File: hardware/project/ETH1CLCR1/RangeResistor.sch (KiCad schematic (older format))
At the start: 107 parts, among them K801 TQ2SA-5V, Q801 BC847W, Q802 2N2218A, Q803 2N2904A, Q804 BC847W, Q805 BC847W, Q806 BC847W, Q807 BC847W, Q808 BC847W, U801 TL072, U802 AD5293BRUZ-20, U803 AQY212GS, U804 HA3-2525-5Z, U805 AQY212GS, U806 AQY212GS, U807 AQY212GS, U808 AQY212GS, U809 AQY212GS, U810 AQY212GS, U811 AQY212GS, U812 AQY212GS, U813 AQY212GS, U814 AQY212GS, U815 AQY212GS

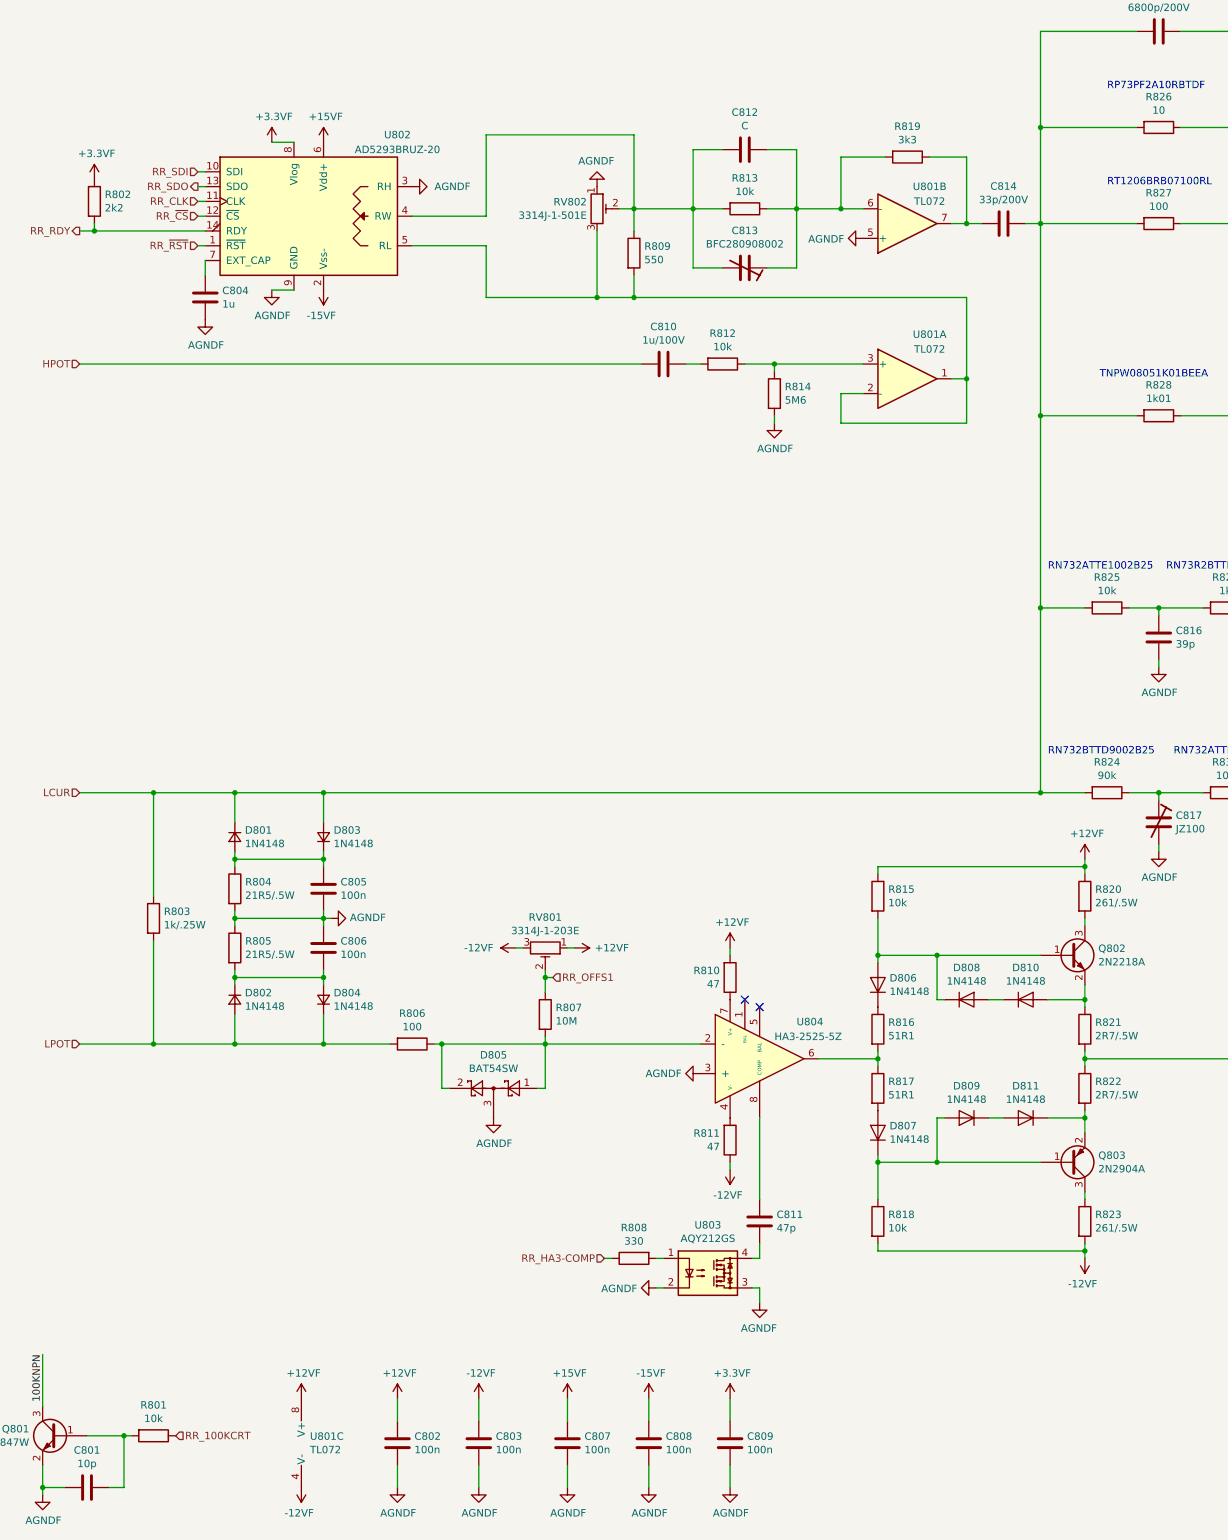
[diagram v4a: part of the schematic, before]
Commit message: Fixed some mistakes in the foorpeints. BOM list ready.
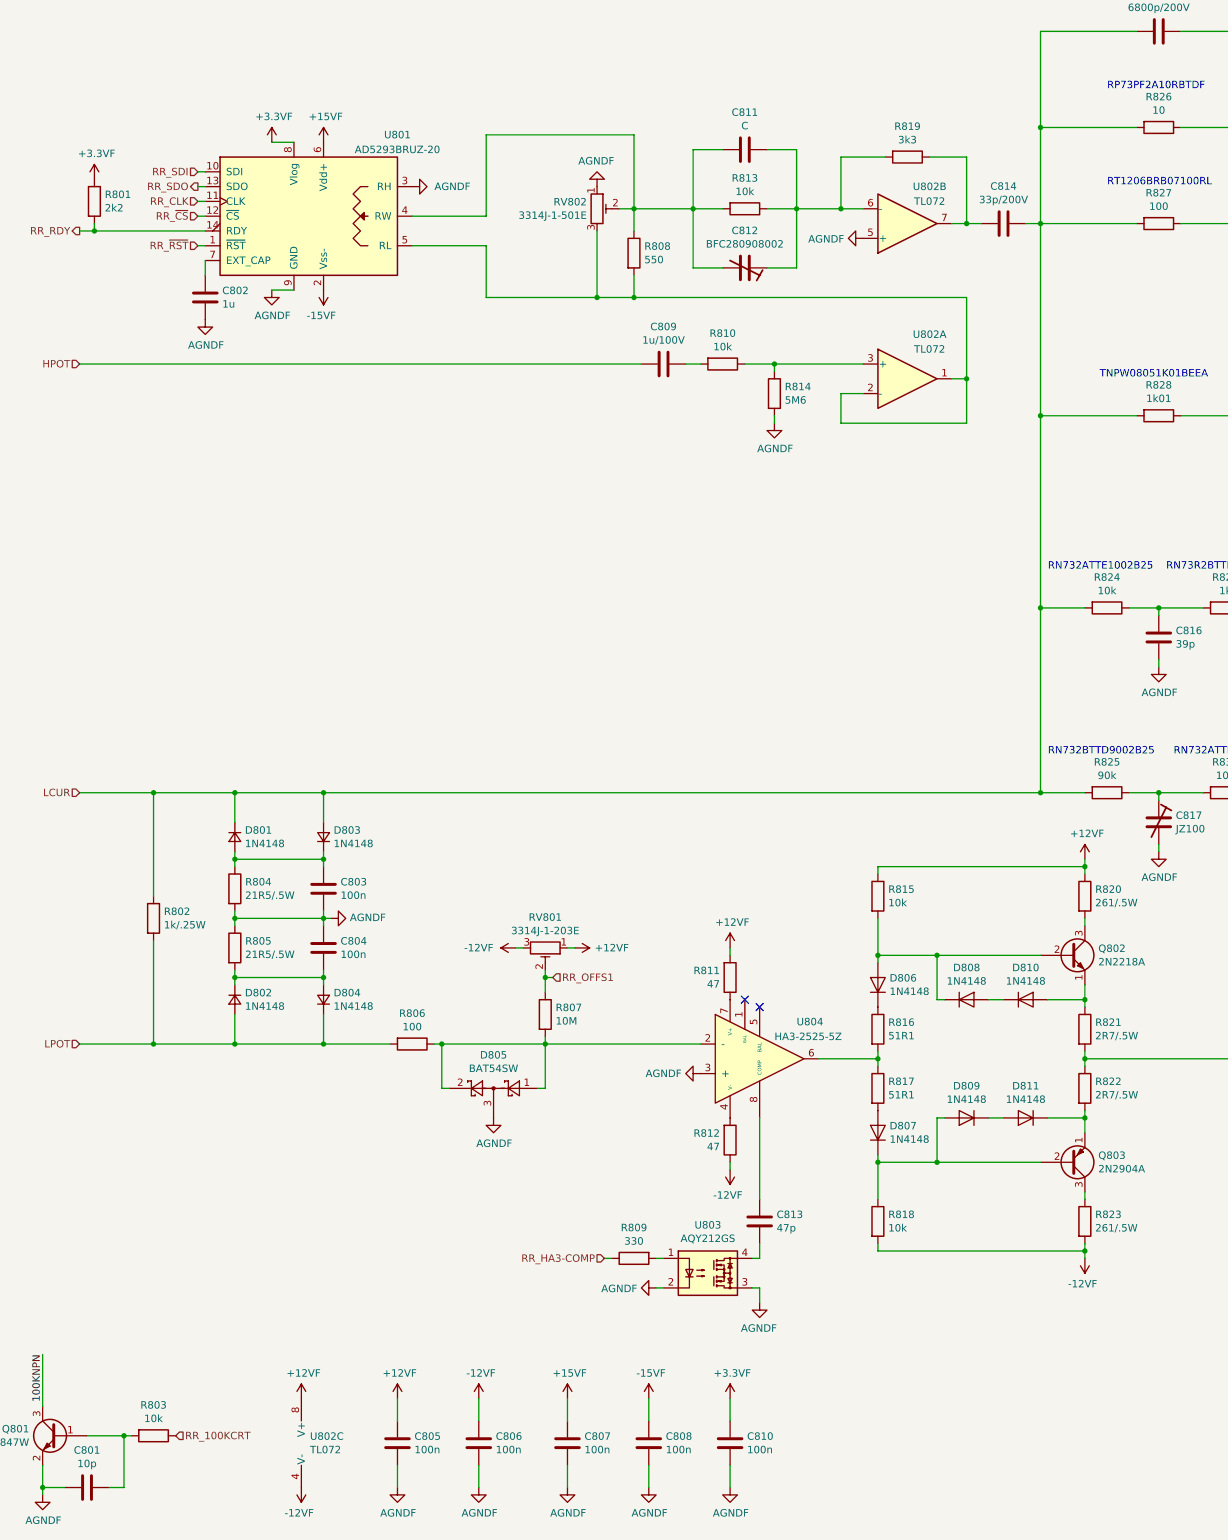
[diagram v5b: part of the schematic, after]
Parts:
- removed Q802: 2N2218A, Package_TO_SOT_THT:TO-39-3, symbol Device:Q_NPN_BEC
- removed Q803: 2N2904A, Package_TO_SOT_THT:TO-39-3, symbol Device:Q_PNP_BEC
- added Q802: 2N2218A, Package_TO_SOT_THT:TO-39-3, symbol Device:Q_NPN_EBC
- added Q803: 2N2904A, Package_TO_SOT_THT:TO-39-3, symbol Device:Q_PNP_EBC
- renumbered C804 to C802, C805 to C803, C806 to C804, C802 to C805, C803 to C806, C810 to C809, C809 to C810, C812 to C811, C813 to C812, C811 to C813, R802 to R801, R803 to R802, R801 to R803, R809 to R808, R808 to R809, R812 to R810, R810 to R811, R811 to R812, R825 to R824, R824 to R825, U802 to U801, U801 to U802
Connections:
- net at D806.2 (A), D808.1 (K), R815.2: now also Q802.2 (B)
- net at D807.1 (K), D809.2 (A), R818.1: now also Q803.2 (B)
- net at D810.2 (A), R821.1: now also Q802.1 (E)
- net at R820.2: now also Q802.3 (C)
- net at D811.1 (K), R822.2: now also Q803.1 (E)
- net at R823.1: now also Q803.3 (C)

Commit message: PCB layout
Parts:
- added C823, C824: 10u/35V, Capacitor_SMD:C_1206_3216Metric_Pad1.42x1.75mm_HandSolder, symbol Device:C
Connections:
- net +12VF: now also C823.1
- net -12VF: now also C824.1
- net AGNDF: now also C823.2, C824.2
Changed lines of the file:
@@
 	6600 9200 6600 9150
 Wire Wire Line
-	8000 9200 6600 9200
+	8000 9200 7350 9200
 Wire Wire Line
 	7000 8600 6600 8600
@@
 $EndComp
 Wire Wire Line
-	6600 6600 8000 6600
+	6600 6600 7350 6600
 Wire Wire Line
 	6600 6650 6600 6600
@@
 	1    0    0    1
 $EndComp
+$Comp
+L Device:C C823
+U 1 1 5E2CBFCE
+P 7350 6800
+F 0 "C823" H 7465 6846 50  0000 L CNN
+F 1 "10u/35V" H 7465 6755 50  0000 L CNN
+F 2 "Capacitor_SMD:C_1206_3216Metric_Pad1.42x1.75mm_HandSolder" H 7388 6650 50  0001 C CNN
+F 3 "~" H 7350 6800 50  0001 C CNN
+	1    7350 6800
+	1    0    0    -1
+$EndComp
+$Comp
+L Device:C C824
+U 1 1 5E2CF1F1
+P 7350 9400
+F 0 "C824" H 7465 9446 50  0000 L CNN
+F 1 "10u/35V" H 7465 9355 50  0000 L CNN
+F 2 "Capacitor_SMD:C_1206_3216Metric_Pad1.42x1.75mm_HandSolder" H 7388 9250 50  0001 C CNN
+F 3 "~" H 7350 9400 50  0001 C CNN
+	1    7350 9400
+	1    0    0    -1
+$EndComp
+Wire Wire Line
+	7350 9250 7350 9200
+Connection ~ 7350 9200
+Wire Wire Line
+	7350 9200 6600 9200
+Wire Wire Line
+	7350 6650 7350 6600
+Connection ~ 7350 6600
+Wire Wire Line
+	7350 6600 8000 6600
+$Comp
+L ETH1CLCR1:AGNDF #PWR0857
+U 1 1 5E30D0CE
+P 7350 9550
+F 0 "#PWR0857" H 7350 9300 50  0001 C CNN
+F 1 "AGNDF" H 7355 9377 50  0000 C CNN
+F 2 "" H 7350 9550 50  0001 C CNN
+F 3 "" H 7350 9550 50  0001 C CNN
+	1    7350 9550
+	-1   0    0    -1
+$EndComp
+$Comp
+L ETH1CLCR1:AGNDF #PWR0856
+U 1 1 5E30DB46
+P 7350 6950
+F 0 "#PWR0856" H 7350 6700 50  0001 C CNN
+F 1 "AGNDF" H 7355 6777 50  0000 C CNN
+F 2 "" H 7350 6950 50  0001 C CNN
+F 3 "" H 7350 6950 50  0001 C CNN
+	1    7350 6950
+	-1   0    0    -1
+$EndComp
 $EndSCHEMATC

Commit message: PCB done.
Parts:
- R842, R843: value 330 -> 680
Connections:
- net +3.3VF: no longer R842.1, R843.1
- net +5VF: now also R842.1, R843.1
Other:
- moved on the sheet: C801, C820, Q801, Q806, R803, R845
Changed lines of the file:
@@
 P 12550 4300
 F 0 "R842" V 12343 4300 50  0000 C CNN
-F 1 "330" V 12434 4300 50  0000 C CNN
+F 1 "680" V 12434 4300 50  0000 C CNN
 F 2 "Resistor_SMD:R_0603_1608Metric_Pad1.05x0.95mm_HandSolder" V 12480 4300 50  0001 C CNN
 F 3 "~" H 12550 4300 50  0001 C CNN
@@
 P 12550 5100
 F 0 "R843" V 12343 5100 50  0000 C CNN
-F 1 "330" V 12434 5100 50  0000 C CNN
+F 1 "680" V 12434 5100 50  0000 C CNN
 F 2 "Resistor_SMD:R_0603_1608Metric_Pad1.05x0.95mm_HandSolder" V 12480 5100 50  0001 C CNN
 F 3 "~" H 12550 5100 50  0001 C CNN
@@
 L Device:R R803
 U 1 1 5E18FE93
-P 1700 10450
-F 0 "R803" V 1493 10450 50  0000 C CNN
-F 1 "10k" V 1584 10450 50  0000 C CNN
-F 2 "Resistor_SMD:R_0603_1608Metric_Pad1.05x0.95mm_HandSolder" V 1630 10450 50  0001 C CNN
-F 3 "~" H 1700 10450 50  0001 C CNN
-	1    1700 10450
-	0    1    1    0
-$EndComp
-Wire Wire Line
-	1550 10450 1500 10450
+P 15150 3900
+F 0 "R803" V 14943 3900 50  0000 C CNN
+F 1 "10k" V 15034 3900 50  0000 C CNN
+F 2 "Resistor_SMD:R_0603_1608Metric_Pad1.05x0.95mm_HandSolder" V 15080 3900 50  0001 C CNN
+F 3 "~" H 15150 3900 50  0001 C CNN
+	1    15150 3900
+	0    1    1    0
+$EndComp
+Wire Wire Line
+	15000 3900 14950 3900
 $Comp
 L Device:C C801
 U 1 1 5E18FE9A
-P 1250 10800
-F 0 "C801" V 998 10800 50  0000 C CNN
-F 1 "10p" V 1089 10800 50  0000 C CNN
-F 2 "Capacitor_SMD:C_0603_1608Metric_Pad1.05x0.95mm_HandSolder" H 1288 10650 50  0001 C CNN
-F 3 "~" H 1250 10800 50  0001 C CNN
-	1    1250 10800
-	0    1    1    0
-$EndComp
-Wire Wire Line
-	1100 10800 950  10800
-Wire Wire Line
-	1400 10800 1500 10800
-Wire Wire Line
-	1500 10800 1500 10450
-Connection ~ 1500 10450
-Wire Wire Line
-	1500 10450 1250 10450
+P 14700 4250
+F 0 "C801" V 14448 4250 50  0000 C CNN
+F 1 "10p" V 14539 4250 50  0000 C CNN
+F 2 "Capacitor_SMD:C_0603_1608Metric_Pad1.05x0.95mm_HandSolder" H 14738 4100 50  0001 C CNN
+F 3 "~" H 14700 4250 50  0001 C CNN
+	1    14700 4250
+	0    1    1    0
+$EndComp
+Wire Wire Line
+	14550 4250 14400 4250
+Wire Wire Line
+	14850 4250 14950 4250
+Wire Wire Line
+	14950 4250 14950 3900
+Connection ~ 14950 3900
+Wire Wire Line
+	14950 3900 14700 3900
 $Comp
 L ETH1CLCR1:AGNDF #PWR0801
 U 1 1 5E18FEA6
-P 950 10850
-F 0 "#PWR0801" H 950 10600 50  0001 C CNN
-F 1 "AGNDF" H 955 10677 50  0000 C CNN
-F 2 "" H 950 10850 50  0001 C CNN
-F 3 "" H 950 10850 50  0001 C CNN
-	1    950  10850
-	1    0    0    -1
-$EndComp
-Wire Wire Line
-	950  10850 950  10800
-Connection ~ 950  10800
-Text HLabel 1850 10450 2    50   Input ~ 0
+P 14400 4300
+F 0 "#PWR0801" H 14400 4050 50  0001 C CNN
+F 1 "AGNDF" H 14405 4127 50  0000 C CNN
+F 2 "" H 14400 4300 50  0001 C CNN
+F 3 "" H 14400 4300 50  0001 C CNN
+	1    14400 4300
+	1    0    0    -1
+$EndComp
+Wire Wire Line
+	14400 4300 14400 4250
+Connection ~ 14400 4250
+Text HLabel 15300 3900 2    50   Input ~ 0
 RR_100KCRT
 Text HLabel 12600 7200 2    50   Input ~ 0
@@
 	1    0    0    1
 $EndComp
-Text Label 950  9900 3    50   ~ 0
+Text Label 14400 3350 3    50   ~ 0
 100KNPN
 Wire Wire Line
-	950  10250 950  9900
+	14400 3700 14400 3350
 Text Label 11250 8900 1    50   ~ 0
 100KNPN
@@
 $EndComp
 $Comp
-L ETH1CLCR1:+3.3VF #PWR0853
-U 1 1 5E73FC90
-P 12700 5100
-F 0 "#PWR0853" H 12700 4950 50  0001 C CNN
-F 1 "+3.3VF" V 12700 5250 50  0000 L CNN
-F 2 "" H 12700 5100 50  0001 C CNN
-F 3 "" H 12700 5100 50  0001 C CNN
-	1    12700 5100
-	0    1    1    0
-$EndComp
-$Comp
-L ETH1CLCR1:+3.3VF #PWR0852
-U 1 1 5E741821
-P 12700 4300
-F 0 "#PWR0852" H 12700 4150 50  0001 C CNN
-F 1 "+3.3VF" V 12700 4450 50  0000 L CNN
-F 2 "" H 12700 4300 50  0001 C CNN
-F 3 "" H 12700 4300 50  0001 C CNN
-	1    12700 4300
-	0    1    1    0
-$EndComp
-$Comp
 L ETH1CLCR1:+3.3VF #PWR0804
 U 1 1 5E74A7BF
@@
 L Device:R R845
 U 1 1 5FDA652B
-P 13450 2450
-F 0 "R845" V 13243 2450 50  0000 C CNN
-F 1 "10k" V 13334 2450 50  0000 C CNN
-F 2 "Resistor_SMD:R_0603_1608Metric_Pad1.05x0.95mm_HandSolder" V 13380 2450 50  0001 C CNN
-F 3 "~" H 13450 2450 50  0001 C CNN
-	1    13450 2450
-	0    1    1    0
-$EndComp
-Wire Wire Line
-	13300 2450 13250 2450
+P 13450 2550
+F 0 "R845" V 13243 2550 50  0000 C CNN
+F 1 "10k" V 13334 2550 50  0000 C CNN
+F 2 "Resistor_SMD:R_0603_1608Metric_Pad1.05x0.95mm_HandSolder" V 13380 2550 50  0001 C CNN
+F 3 "~" H 13450 2550 50  0001 C CNN
+	1    13450 2550
+	0    1    1    0
+$EndComp
+Wire Wire Line
+	13300 2550 13250 2550
 $Comp
 L Device:C C820
 U 1 1 5FDA6532
-P 13000 2800
-F 0 "C820" V 12748 2800 50  0000 C CNN
-F 1 "10p" V 12839 2800 50  0000 C CNN
-F 2 "Capacitor_SMD:C_0603_1608Metric_Pad1.05x0.95mm_HandSolder" H 13038 2650 50  0001 C CNN
-F 3 "~" H 13000 2800 50  0001 C CNN
-	1    13000 2800
-	0    1    1    0
-$EndComp
-Wire Wire Line
-	12850 2800 12700 2800
-Wire Wire Line
-	12700 2800 12700 2650
-Wire Wire Line
-	13150 2800 13250 2800
-Wire Wire Line
-	13250 2800 13250 2450
-Connection ~ 13250 2450
-Wire Wire Line
-	13250 2450 13000 2450
+P 13000 2900
+F 0 "C820" V 12748 2900 50  0000 C CNN
+F 1 "10p" V 12839 2900 50  0000 C CNN
+F 2 "Capacitor_SMD:C_0603_1608Metric_Pad1.05x0.95mm_HandSolder" H 13038 2750 50  0001 C CNN
+F 3 "~" H 13000 2900 50  0001 C CNN
+	1    13000 2900
+	0    1    1    0
+$EndComp
+Wire Wire Line
+	12850 2900 12700 2900
+Wire Wire Line
+	12700 2900 12700 2750
+Wire Wire Line
+	13150 2900 13250 2900
+Wire Wire Line
+	13250 2900 13250 2550
+Connection ~ 13250 2550
+Wire Wire Line
+	13250 2550 13000 2550
 $Comp
 L ETH1CLCR1:AGNDF #PWR0851
 U 1 1 5FDA653E
-P 12700 2850
-F 0 "#PWR0851" H 12700 2600 50  0001 C CNN
-F 1 "AGNDF" H 12705 2677 50  0000 C CNN
-F 2 "" H 12700 2850 50  0001 C CNN
-F 3 "" H 12700 2850 50  0001 C CNN
-	1    12700 2850
-	1    0    0    -1
-$EndComp
-Wire Wire Line
-	12700 2850 12700 2800
-Connection ~ 12700 2800
-Wire Wire Line
-	12700 2250 12700 1900
+P 12700 2950
+F 0 "#PWR0851" H 12700 2700 50  0001 C CNN
+F 1 "AGNDF" H 12705 2777 50  0000 C CNN
+F 2 "" H 12700 2950 50  0001 C CNN
+F 3 "" H 12700 2950 50  0001 C CNN
+	1    12700 2950
+	1    0    0    -1
+$EndComp
+Wire Wire Line
+	12700 2950 12700 2900
+Connection ~ 12700 2900
+Wire Wire Line
+	12700 2350 12700 2000
 $Comp
 L Transistor_BJT:BC847W Q808
@@
 Text HLabel 15300 1200 2    50   Input ~ 0
 RR_100CRT
-Text HLabel 13600 2450 2    50   Input ~ 0
+Text HLabel 13600 2550 2    50   Input ~ 0
 RR_1KCRT
 Text HLabel 15300 2550 2    50   Input ~ 0
@@
 Text Label 12700 650  3    50   ~ 0
 R10NPN
-Text Label 12700 1900 3    50   ~ 0
+Text Label 12700 2000 3    50   ~ 0
 R1KNPN
 Text Label 9700 1450 0    50   ~ 0
@@
 $EndComp
 Wire Wire Line
-	950  10800 950  10650
+	14400 4250 14400 4100
 $Comp
 L Transistor_BJT:BC847W Q801
 U 1 1 605ADF1E
-P 1050 10450
-F 0 "Q801" H 1241 10496 50  0000 L CNN
-F 1 "BC847W" H 1241 10405 50  0000 L CNN
-F 2 "Package_TO_SOT_SMD:SOT-323_SC-70" H 1250 10375 50  0001 L CIN
-F 3 "http://www.infineon.com/dgdl/Infineon-BC847SERIES_BC848SERIES_BC849SERIES_BC850SERIES-DS-v01_01-en.pdf?fileId=db3a304314dca389011541d4630a1657" H 1050 10450 50  0001 L CNN
-	1    1050 10450
+P 14500 3900
+F 0 "Q801" H 14691 3946 50  0000 L CNN
+F 1 "BC847W" H 14691 3855 50  0000 L CNN
+F 2 "Package_TO_SOT_SMD:SOT-323_SC-70" H 14700 3825 50  0001 L CIN
+F 3 "http://www.infineon.com/dgdl/Infineon-BC847SERIES_BC848SERIES_BC849SERIES_BC850SERIES-DS-v01_01-en.pdf?fileId=db3a304314dca389011541d4630a1657" H 14500 3900 50  0001 L CNN
+	1    14500 3900
 	-1   0    0    -1
 $EndComp
@@
 L Transistor_BJT:BC847W Q806
 U 1 1 5FDA6525
-P 12800 2450
-F 0 "Q806" H 12500 2650 50  0000 L CNN
-F 1 "BC847W" H 12400 2550 50  0000 L CNN
-F 2 "Package_TO_SOT_SMD:SOT-323_SC-70" H 13000 2375 50  0001 L CIN
-F 3 "http://www.infineon.com/dgdl/Infineon-BC847SERIES_BC848SERIES_BC849SERIES_BC850SERIES-DS-v01_01-en.pdf?fileId=db3a304314dca389011541d4630a1657" H 12800 2450 50  0001 L CNN
-	1    12800 2450
+P 12800 2550
+F 0 "Q806" H 12500 2750 50  0000 L CNN
+F 1 "BC847W" H 12400 2650 50  0000 L CNN
+F 2 "Package_TO_SOT_SMD:SOT-323_SC-70" H 13000 2475 50  0001 L CIN
+F 3 "http://www.infineon.com/dgdl/Infineon-BC847SERIES_BC848SERIES_BC849SERIES_BC850SERIES-DS-v01_01-en.pdf?fileId=db3a304314dca389011541d4630a1657" H 12800 2550 50  0001 L CNN
+	1    12800 2550
 	-1   0    0    -1
 $EndComp
@@
 	-1   0    0    -1
 $EndComp
+$Comp
+L ETH1CLCR1:+5VF #PWR0106
+U 1 1 5E5DA381
+P 12700 4300
+F 0 "#PWR0106" H 12700 4150 50  0001 C CNN
+F 1 "+5VF" V 12700 4450 50  0000 L CNN
+F 2 "" H 12700 4300 50  0001 C CNN
+F 3 "" H 12700 4300 50  0001 C CNN
+	1    12700 4300
+	0    1    1    0
+$EndComp
+$Comp
+L ETH1CLCR1:+5VF #PWR0107
+U 1 1 5E5DDA44
+P 12700 5100
+F 0 "#PWR0107" H 12700 4950 50  0001 C CNN
+F 1 "+5VF" V 12700 5250 50  0000 L CNN
+F 2 "" H 12700 5100 50  0001 C CNN
+F 3 "" H 12700 5100 50  0001 C CNN
+	1    12700 5100
+	0    1    1    0
+$EndComp
 $EndSCHEMATC

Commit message: Small changes in schematics and PCB
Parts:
- R809, R840: value 330 -> 680
- R824, R830: value 10k -> 10k/.1%
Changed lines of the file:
@@
 P 8150 4850
 F 0 "R824" V 7943 4850 50  0000 C CNN
-F 1 "10k" V 8034 4850 50  0000 C CNN
+F 1 "10k/.1%" V 8034 4850 50  0000 C CNN
 F 2 "Resistor_SMD:R_0603_1608Metric_Pad1.05x0.95mm_HandSolder" V 8080 4850 50  0001 C CNN
 F 3 "~" H 8150 4850 50  0001 C CNN
@@
 P 11050 8700
 F 0 "R840" H 10981 8654 50  0000 R CNN
-F 1 "330" H 10981 8745 50  0000 R CNN
+F 1 "680" H 10981 8745 50  0000 R CNN
 F 2 "Resistor_SMD:R_0603_1608Metric_Pad1.05x0.95mm_HandSolder" V 10980 8700 50  0001 C CNN
 F 3 "~" H 11050 8700 50  0001 C CNN
@@
 P 4950 9250
 F 0 "R809" V 4743 9250 50  0000 C CNN
-F 1 "330" V 4834 9250 50  0000 C CNN
+F 1 "680" V 4834 9250 50  0000 C CNN
 F 2 "Resistor_SMD:R_0603_1608Metric_Pad1.05x0.95mm_HandSolder" V 4880 9250 50  0001 C CNN
 F 3 "~" H 4950 9250 50  0001 C CNN
@@
 P 8950 6100
 F 0 "R830" V 8743 6100 50  0000 C CNN
-F 1 "10k" V 8834 6100 50  0000 C CNN
+F 1 "10k/.1%" V 8834 6100 50  0000 C CNN
 F 2 "Resistor_SMD:R_0603_1608Metric_Pad1.05x0.95mm_HandSolder" V 8880 6100 50  0001 C CNN
 F 3 "~" H 8950 6100 50  0001 C CNN
